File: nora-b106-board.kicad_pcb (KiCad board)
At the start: 2 copper layers, 36 x 36 mm, 15 parts, among them J1 TYPE-C-31-M-12, J2 SWD / PICO, J3 GPIO 3V3, SW1 RESET, U1 NORA-B106-00B, U2 XC6206P332MR-G, U3 USBLC6-2SC6

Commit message: Improve module grounding and fix nRF53 programmer setup for revision B
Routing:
- net /P1.13_RX: track 33.5 -> 79.7 mm
- net /GND: track 51.8 -> 42.1 mm, vias 16 -> 36
- net /SWDIO: track 28.5 -> 38.1 mm
- net /RESET_N: track 54.3 -> 63.8 mm
- net /SWCLK: track 34.8 -> 43.8 mm, vias 1 -> 2
- net /VBUS: track 59.0 -> 59.8 mm
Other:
- board text added: "NORA-B106 rev B"
- board text removed: "NORA-B106 rev A"

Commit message: Expose six more GPIOs on optional headers in revision C
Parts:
- added J4: EXTRA GPIO, Breakout:PinHeader_1x04_P2.54mm_Vertical, F.Cu at (106.7, 113.3)
- added J5: EXTRA GPIO, Breakout:PinHeader_1x02_P2.54mm_Vertical, F.Cu at (134.4, 106.7)
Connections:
- U1 pad D1: unconnected-(U1B-P0.15-PadD1) -> /P0.15
- U1 pad E1: unconnected-(U1B-P0.18-PadE1) -> /P0.18
- U1 pad E9: unconnected-(U1B-P1.05-PadE9) -> /P1.05
- U1 pad F9: unconnected-(U1B-P1.15-PadF9) -> /P1.15
- U1 pad H9: unconnected-(U1B-P1.11-PadH9) -> /P1.11
- U1 pad J9: unconnected-(U1B-P0.31-PadJ9) -> /P0.31
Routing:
- net /P0.31: track 0.00 -> 23.4 mm
- net /P1.05: track 0.00 -> 15.6 mm
- net /P1.15: track 0.00 -> 15.1 mm
- net /P1.11: track 0.00 -> 13.5 mm, vias 0 -> 1
- net /P0.18: track 0.00 -> 13.1 mm
- net /P0.15: track 0.00 -> 12.5 mm
- net /+3V3: track 57.4 -> 59.3 mm, vias 2 -> 4
- net /LED_A: track 4.86 -> 6.27 mm
- net /GND: vias 36 -> 35
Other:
- board text added: "J2: 1=3V3 2=GND 3=CLK 4=DIO 5=RST J3: 1=3V3 2=GND 3=P1.12 4=P1.13 5=P0.04 6=P0.05 7=P1.02 8=P1.03 J4: 1=P0.31 2=P1.11 3=P1.15 4=P1.05 J5: 1=P0.18 2=P0.15 USB POWER / 3V3 I/O"
- board text added: "NORA-B106 rev C"
- board text added: "P0.15"
- board text added: "P0.18"
- board text added: "P0.31"
- board text added: "P1.05"
- board text added: "P1.11"
- board text added: "P1.15"
- board text removed: "J2: 1=3V3 2=GND 3=CLK 4=DIO 5=RST J3: 1=3V3 2=GND 3=P1.12 4=P1.13 5=P0.04 6=P0.05 7=P1.02 8=P1.03 USB POWER / 3V3 I/O"
- board text removed: "NORA-B106 rev B"

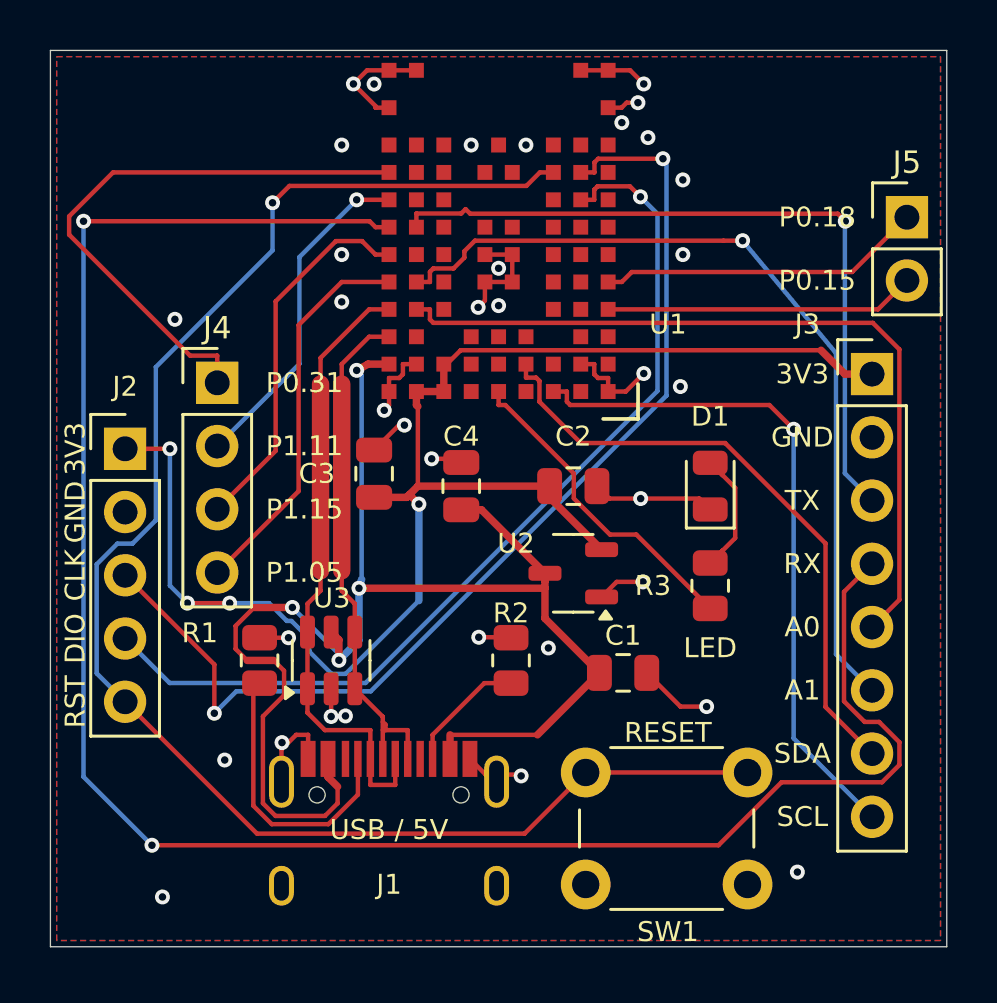
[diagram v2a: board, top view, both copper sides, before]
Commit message: Consolidate GPIOs into one right-edge header in revision D
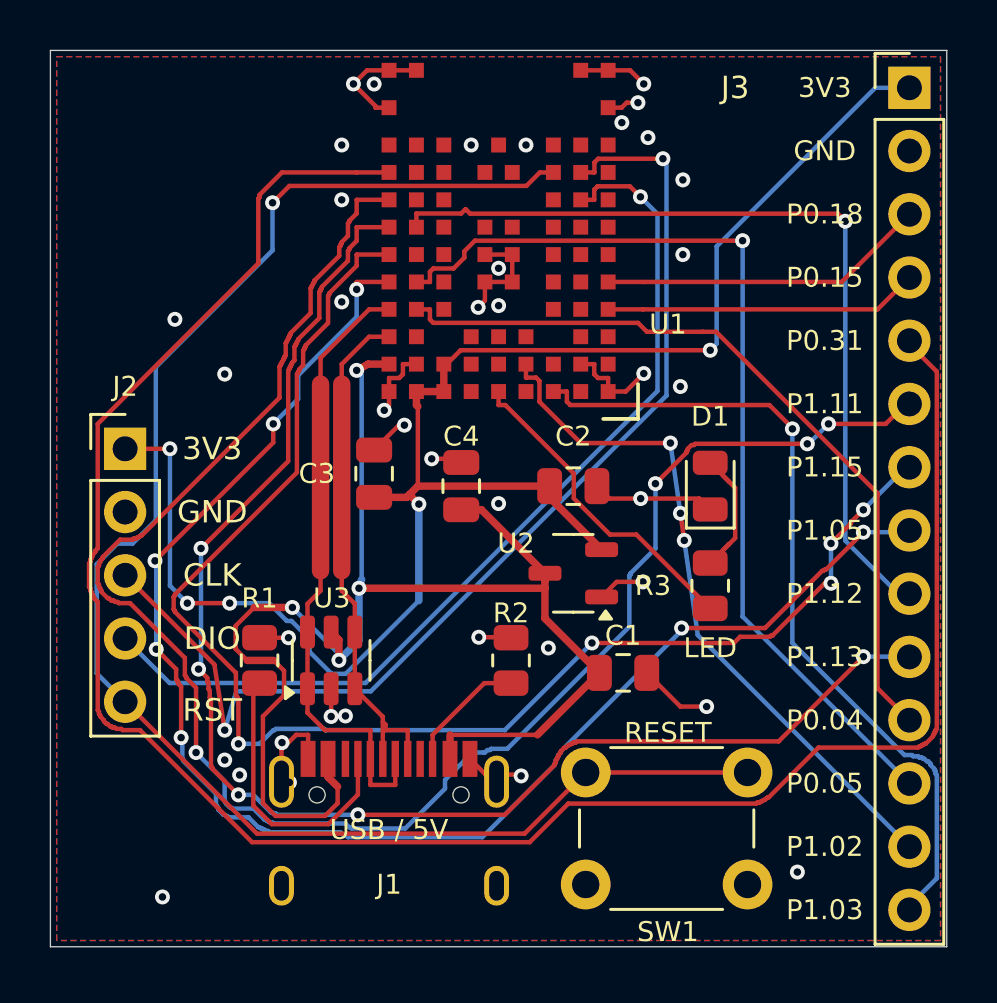
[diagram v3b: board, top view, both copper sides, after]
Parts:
- removed J4: EXTRA GPIO, Breakout:PinHeader_1x04_P2.54mm_Vertical
- removed J5: EXTRA GPIO, Breakout:PinHeader_1x02_P2.54mm_Vertical
- J3: value GPIO 3V3 -> GPIO / 3V3; footprint Breakout:PinHeader_1x08_P2.54mm_Vertical -> Breakout:PinHeader_1x14_P2.54mm_Vertical
- moved J3 11.6 mm to (134.5, 101.5)
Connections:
- J3 pad 3: /P1.12_TX -> /P0.18
- J3 pad 4: /P1.13_RX -> /P0.15
- J3 pad 5: /P0.04_AIN0 -> /P0.31
- J3 pad 6: /P0.05_AIN1 -> /P1.11
- J3 pad 7: /P1.02_SDA -> /P1.15
- J3 pad 8: /P1.03_SCL -> /P1.05
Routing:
- net /P0.31: track 23.4 -> 83.3 mm
- net /P1.11: track 13.5 -> 70.8 mm, vias 1 -> 4
- net /P1.05: track 15.6 -> 60.4 mm, vias 0 -> 7
- net /P1.15: track 15.1 -> 57.6 mm, vias 0 -> 5
- net /P1.13_RX: track 79.7 -> 57.5 mm, vias 2 -> 5
- net /+3V3: track 59.3 -> 67.0 mm, vias 4 -> 5
- net /P1.03_SCL: track 27.4 -> 33.2 mm
- net /P1.12_TX: track 29.7 -> 34.3 mm
- net /P0.05_AIN1: track 34.2 -> 38.7 mm
- net /P1.02_SDA: track 25.0 -> 27.7 mm, vias 0 -> 3
- net /SWCLK: track 43.8 -> 44.9 mm
- net /LED_A: track 6.27 -> 5.56 mm
- net /GND: vias 35 -> 39
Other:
- board text added: "J2: 1=3V3 2=GND 3=CLK 4=DIO 5=RST J3: 12 GPIO + 3V3/GND 3V3 I/O ONLY USB POWER: 5V"
- board text added: "NORA-B106 rev D"
- board text added: "P0.04"
- board text added: "P0.05"
- board text added: "P1.02"
- board text added: "P1.03"
- board text added: "P1.12"
- board text added: "P1.13"
- board text removed: "A0"
- board text removed: "A1"
- board text removed: "J2: 1=3V3 2=GND 3=CLK 4=DIO 5=RST J3: 1=3V3 2=GND 3=P1.12 4=P1.13 5=P0.04 6=P0.05 7=P1.02 8=P1.03 J4: 1=P0.31 2=P1.11 3=P1.15 4=P1.05 J5: 1=P0.18 2=P0.15 USB POWER / 3V3 I/O"
- board text removed: "NORA-B106 rev C"
- board text removed: "RX"
- board text removed: "SCL"
- board text removed: "SDA"
- board text removed: "TX"
